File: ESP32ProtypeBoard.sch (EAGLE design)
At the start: 88 parts, among them IC2 SI4431BDY, J10 POWER_JACKPTH_LOCK, Q2 MMBT3904, Q3 MMBT3904, Q4 BSS138, U2 ESP-WROOM-32

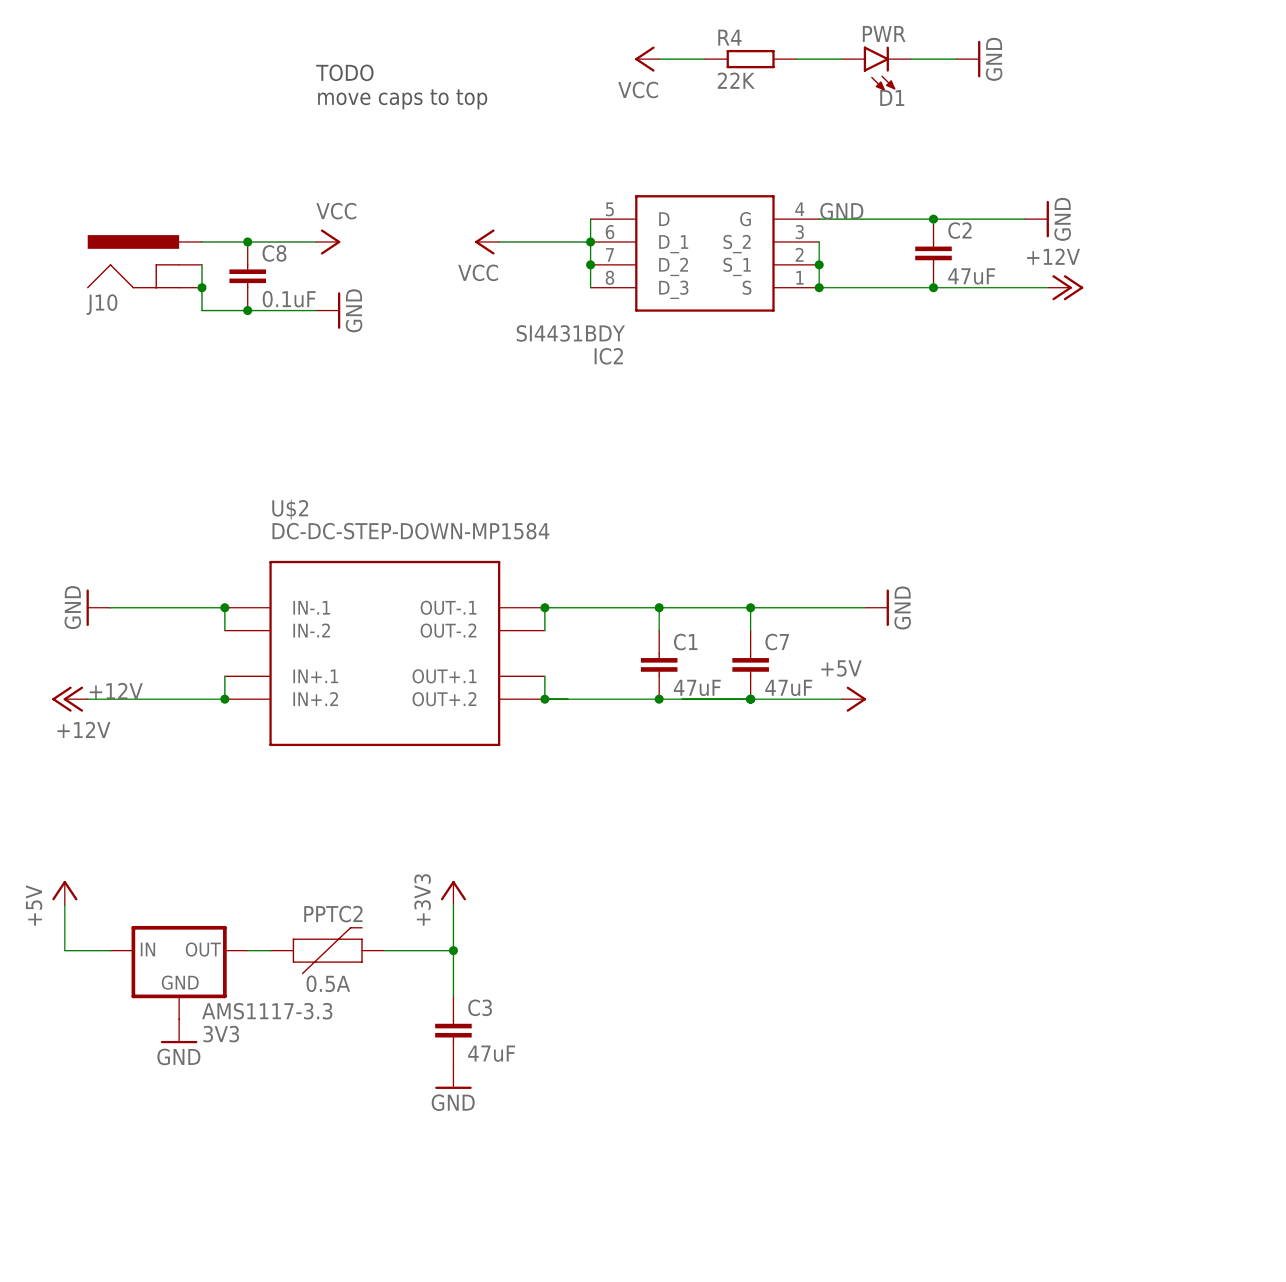
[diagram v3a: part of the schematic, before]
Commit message: Replaced buck converter module with custom curcuit
Using ACT4088US-T for 5V rail
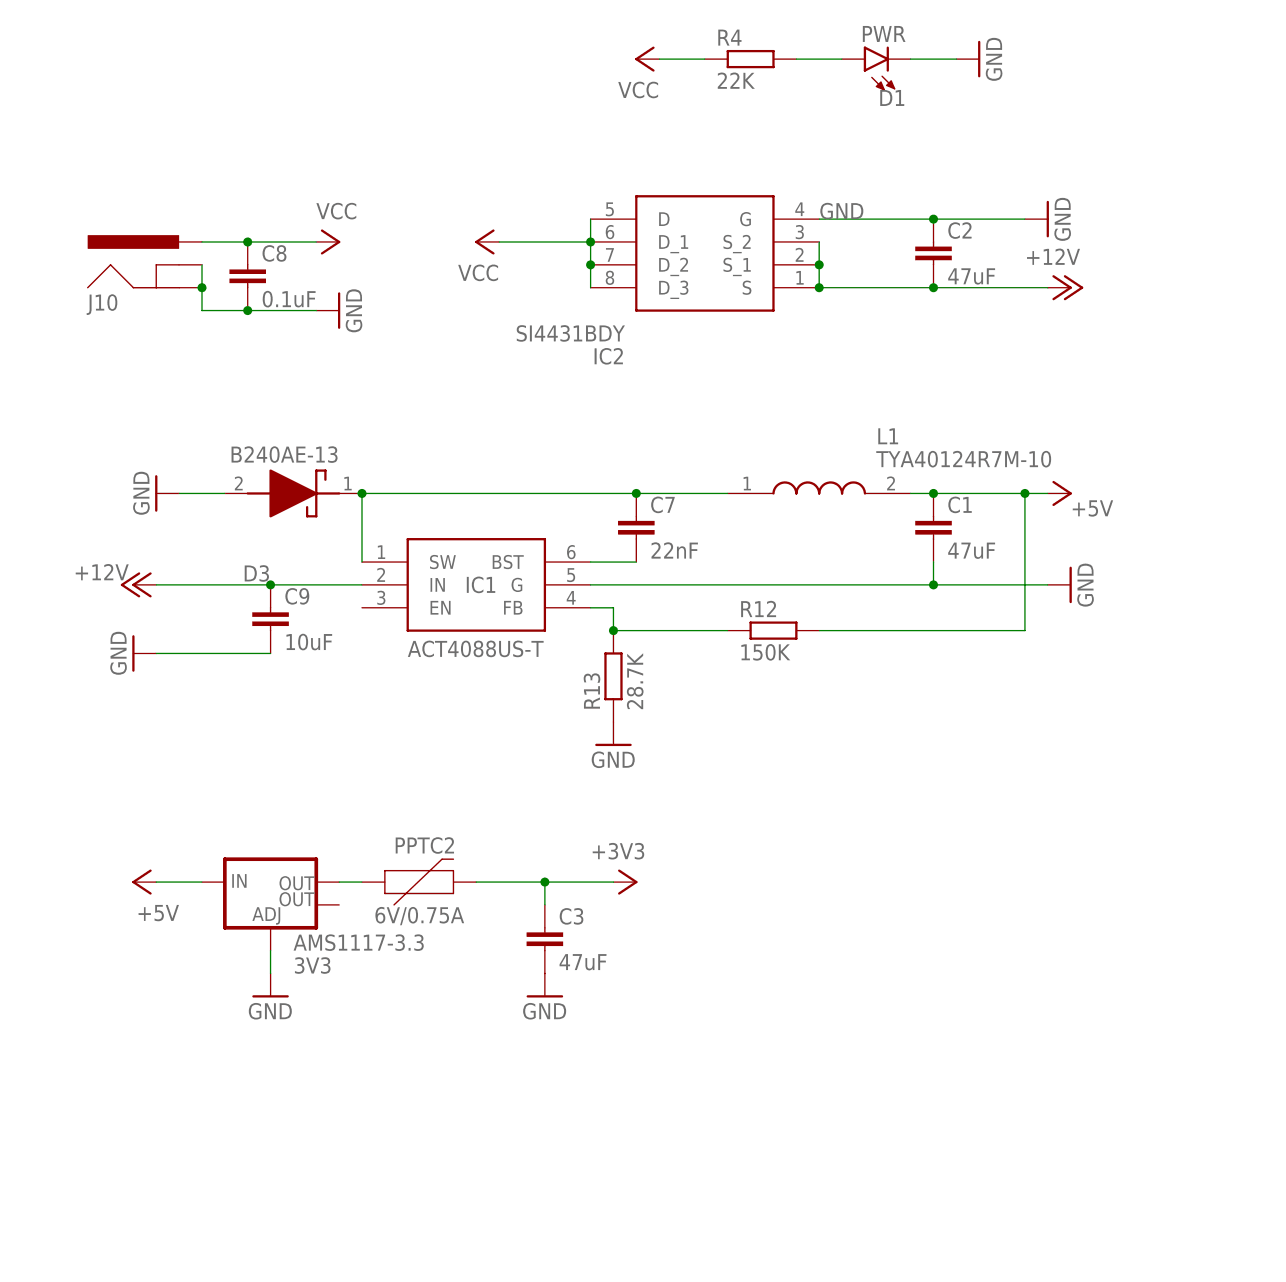
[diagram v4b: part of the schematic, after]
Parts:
- removed U$2: DC-DC-STEP-DOWN-MP1584, diy-modules-modified:DC-DC-STEP-DOWN-MP1584
- added C9: 10uF, rcl:C-EUC0805K
- added D3: B240AE-13, B240AE-13:B240AE-13
- added IC1: ACT4088US-T, ACT4088US-T:ACT4088US-T
- added L1: TYA40124R7M-10, TYA40124R7M-10:TYA40124R7M-10
- added R12: 150K, rcl:R-EU_R0805
- added R13: 28.7K, rcl:R-EU_R0805
- AMS1117-3.3: device SparkFun-IC-Power:V_REG_LD1117VXXLD1117-SMD -> SparkFun-IC-Power:V_REG_LM1117SOT223
- C7: value 47uF -> 22nF; device rcl:C-EUC1206K -> rcl:C-EUC0805K
- PPTC2: value 0.5A -> 6V/0.75A; device SparkFun-Fuses:PPTC_0.75A -> SparkFun-Fuses:PPTC_THREE-QUARTER-AMP
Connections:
- new net N$13: C7.1, D3.K, IC1.SW, L1.1
- new net N$14: C7.2, IC1.BST
- new net N$17: IC1.FB, R12.1, R13.2
- net +12V: now also C9.1, IC1.IN; no longer U$2.IN+.1, U$2.IN+.2
- net +5V: now also C1.1, L1.2, R12.2; no longer C1.2, C7.2, U$2.OUT+.1, U$2.OUT+.2
- net GND: now also AMS1117-3.3.ADJ, C1.2, C9.2, D3.A, IC1.G, R13.1; no longer AMS1117-3.3.GND, C1.1, C7.1, U$2.IN-.1, U$2.IN-.2, U$2.OUT-.1, U$2.OUT-.2
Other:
- note removed: "TODO move caps to top"
- moved on the sheet: C1, C3, C7

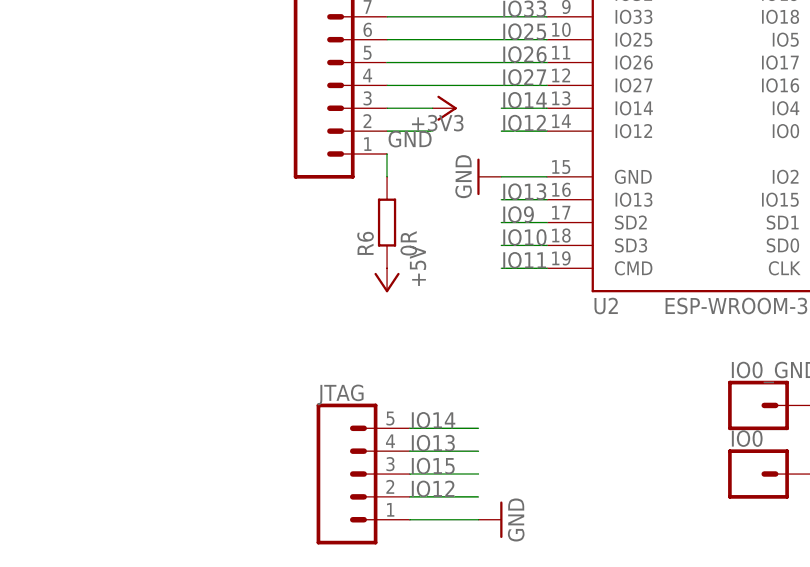
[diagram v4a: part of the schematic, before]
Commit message: Replaced all resistors with 0805 variants
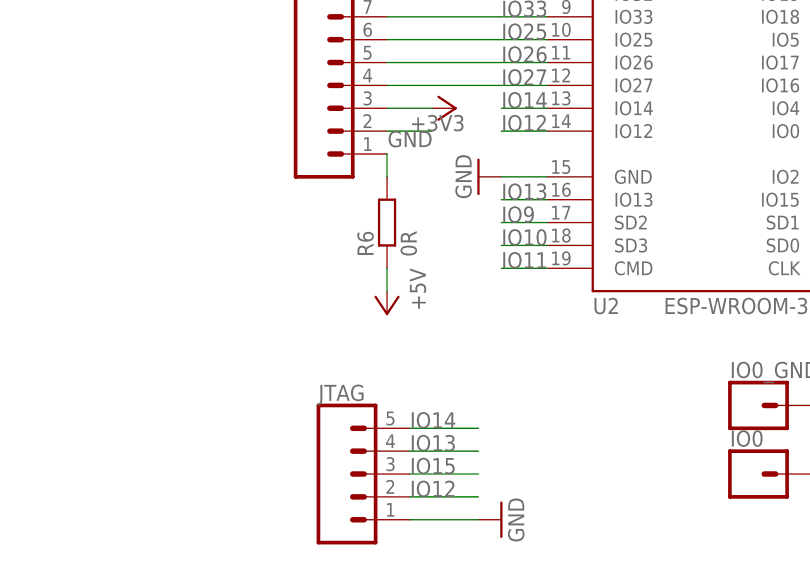
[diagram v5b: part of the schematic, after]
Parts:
- C4: device rcl:C-EUC1206 -> rcl:C-EUC0805K
- R1, R10, R11, R2, R3, R4, R5, R7, R8, R9: device eagle-ltspice:RR1206 -> rcl:R-EU_R0805
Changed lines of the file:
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@@
 <part name="GND2" library="supply1" library_urn="urn:adsk.eagle:library:371" deviceset="GND" device=""/>
 <part name="+3V1" library="supply1" library_urn="urn:adsk.eagle:library:371" deviceset="+3V3" device=""/>
-<part name="C4" library="rcl" library_urn="urn:adsk.eagle:library:334" deviceset="C-EU" device="C1206" package3d_urn="urn:adsk.eagle:package:23618/2" value="22uF"/>
+<part name="C4" library="rcl" library_urn="urn:adsk.eagle:library:334" deviceset="C-EU" device="C0805K" package3d_urn="urn:adsk.eagle:package:23681/2" value="22uF"/>
 <part name="C5" library="rcl" library_urn="urn:adsk.eagle:library:334" deviceset="C-EU" device="C0805K" package3d_urn="urn:adsk.eagle:package:23681/2" value="0.1uF"/>
-<part name="R5" library="eagle-ltspice" library_urn="urn:adsk.eagle:library:217" deviceset="R" device="R1206" package3d_urn="urn:adsk.eagle:package:13301/1" value="10K"/>
+<part name="R5" library="rcl" library_urn="urn:adsk.eagle:library:334" deviceset="R-EU_" device="R0805" package3d_urn="urn:adsk.eagle:package:23553/2" value="10K"/>
 <part name="C6" library="rcl" library_urn="urn:adsk.eagle:library:334" deviceset="C-EU" device="C0805K" package3d_urn="urn:adsk.eagle:package:23681/2" value="1nF"/>
 <part name="GND6" library="supply1" library_urn="urn:adsk.eagle:library:371" deviceset="GND" device=""/>
@@
 <part name="UART" library="SparkFun-Connectors" library_urn="urn:adsk.eagle:library:513" deviceset="CONN_06" device="LOCK" package3d_urn="urn:adsk.eagle:package:38002/1"/>
 <part name="GND20" library="supply1" library_urn="urn:adsk.eagle:library:371" deviceset="GND" device=""/>
-<part name="R7" library="eagle-ltspice" library_urn="urn:adsk.eagle:library:217" deviceset="R" device="R1206" package3d_urn="urn:adsk.eagle:package:13301/1" value="470R"/>
-<part name="R8" library="eagle-ltspice" library_urn="urn:adsk.eagle:library:217" deviceset="R" device="R1206" package3d_urn="urn:adsk.eagle:package:13301/1" value="470R"/>
+<part name="R7" library="rcl" library_urn="urn:adsk.eagle:library:334" deviceset="R-EU_" device="R0805" package3d_urn="urn:adsk.eagle:package:23553/2" value="470R"/>
+<part name="R8" library="rcl" library_urn="urn:adsk.eagle:library:334" deviceset="R-EU_" device="R0805" package3d_urn="urn:adsk.eagle:package:23553/2" value="470R"/>
 <part name="GND1" library="supply1" library_urn="urn:adsk.eagle:library:371" deviceset="GND" device=""/>
 <part name="AMS1117-3.3" library="SparkFun-IC-Power" library_urn="urn:adsk.eagle:library:526" deviceset="V_REG_LM1117" device="SOT223" package3d_urn="urn:adsk.eagle:package:39069/1" value="3V3"/>
@@
 <part name="P+8" library="supply1" library_urn="urn:adsk.eagle:library:371" deviceset="+12V" device=""/>
 <part name="D2" library="SparkFun-LED" deviceset="LED-GREEN" device="1206" value="GREEN"/>
-<part name="R1" library="eagle-ltspice" library_urn="urn:adsk.eagle:library:217" deviceset="R" device="R1206" package3d_urn="urn:adsk.eagle:package:13301/1" value="10K"/>
+<part name="R1" library="rcl" library_urn="urn:adsk.eagle:library:334" deviceset="R-EU_" device="R0805" package3d_urn="urn:adsk.eagle:package:23553/2" value="10K"/>
 <part name="J5" library="SparkFun-Connectors" library_urn="urn:adsk.eagle:library:513" deviceset="CONN_17" device="NOSILK" package3d_urn="urn:adsk.eagle:package:38192/1"/>
 <part name="J8" library="SparkFun-Connectors" library_urn="urn:adsk.eagle:library:513" deviceset="CONN_12" device="NO_SILK" package3d_urn="urn:adsk.eagle:package:38179/1"/>
-<part name="R2" library="eagle-ltspice" library_urn="urn:adsk.eagle:library:217" deviceset="R" device="R1206" package3d_urn="urn:adsk.eagle:package:13301/1" value="10K"/>
+<part name="R2" library="rcl" library_urn="urn:adsk.eagle:library:334" deviceset="R-EU_" device="R0805" package3d_urn="urn:adsk.eagle:package:23553/2" value="10K"/>
 <part name="+3V2" library="supply1" library_urn="urn:adsk.eagle:library:371" deviceset="+3V3" device=""/>
 <part name="P+11" library="supply1" library_urn="urn:adsk.eagle:library:371" deviceset="VCC" device=""/>
@@
 <part name="Q2" library="semicon-smd-ipc" library_urn="urn:adsk.eagle:library:353" deviceset="NPN-TRANSISTOR_" device="SOT23" package3d_urn="urn:adsk.eagle:package:28738/2" value="MMBT3904"/>
 <part name="Q3" library="semicon-smd-ipc" library_urn="urn:adsk.eagle:library:353" deviceset="NPN-TRANSISTOR_" device="SOT23" package3d_urn="urn:adsk.eagle:package:28738/2" value="MMBT3904"/>
-<part name="R3" library="eagle-ltspice" library_urn="urn:adsk.eagle:library:217" deviceset="R" device="R1206" package3d_urn="urn:adsk.eagle:package:13301/1" value="10K"/>
-<part name="R10" library="eagle-ltspice" library_urn="urn:adsk.eagle:library:217" deviceset="R" device="R1206" package3d_urn="urn:adsk.eagle:package:13301/1" value="10K"/>
+<part name="R3" library="rcl" library_urn="urn:adsk.eagle:library:334" deviceset="R-EU_" device="R0805" package3d_urn="urn:adsk.eagle:package:23553/2" value="10K"/>
+<part name="R10" library="rcl" library_urn="urn:adsk.eagle:library:334" deviceset="R-EU_" device="R0805" package3d_urn="urn:adsk.eagle:package:23553/2" value="10K"/>
 <part name="J56" library="SparkFun-Connectors" library_urn="urn:adsk.eagle:library:513" deviceset="CONN_11" device="1X11_NO_SILK" package3d_urn="urn:adsk.eagle:package:38260/1"/>
 <part name="J57" library="SparkFun-Connectors" library_urn="urn:adsk.eagle:library:513" deviceset="CONN_02" device="1X02_NO_SILK" package3d_urn="urn:adsk.eagle:package:38051/1"/>
 <part name="P+3" library="supply1" library_urn="urn:adsk.eagle:library:371" deviceset="VCC" device=""/>
-<part name="R4" library="eagle-ltspice" library_urn="urn:adsk.eagle:library:217" deviceset="R" device="R1206" package3d_urn="urn:adsk.eagle:package:13301/1" value="22K"/>
+<part name="R4" library="rcl" library_urn="urn:adsk.eagle:library:334" deviceset="R-EU_" device="R0805" package3d_urn="urn:adsk.eagle:package:23553/2" value="22K"/>
 <part name="D1" library="SparkFun-LED" deviceset="LED-GREEN" device="1206" value="PWR"/>
 <part name="GND5" library="supply1" library_urn="urn:adsk.eagle:library:371" deviceset="GND" device=""/>
@@
 <part name="SMD8" library="eagle-ltspice" library_urn="urn:adsk.eagle:library:217" deviceset="R" device="R1206" package3d_urn="urn:adsk.eagle:package:13301/1"/>
 <part name="Q1" library="semicon-smd-ipc" library_urn="urn:adsk.eagle:library:353" deviceset="NPN-TRANSISTOR_" device="SOT23" package3d_urn="urn:adsk.eagle:package:28738/2"/>
-<part name="R9" library="eagle-ltspice" library_urn="urn:adsk.eagle:library:217" deviceset="R" device="R1206" package3d_urn="urn:adsk.eagle:package:13301/1" value="100K"/>
+<part name="R9" library="rcl" library_urn="urn:adsk.eagle:library:334" deviceset="R-EU_" device="R0805" package3d_urn="urn:adsk.eagle:package:23553/2" value="100K"/>
 <part name="+3V6" library="supply1" library_urn="urn:adsk.eagle:library:371" deviceset="+3V3" device=""/>
 <part name="P+7" library="supply1" library_urn="urn:adsk.eagle:library:371" deviceset="+5V" device=""/>
@@
 <part name="GND14" library="supply1" library_urn="urn:adsk.eagle:library:371" deviceset="GND" device=""/>
 <part name="J2" library="SparkFun-Connectors" library_urn="urn:adsk.eagle:library:513" deviceset="CONN_03" device="LOCK_NO_SILK" package3d_urn="urn:adsk.eagle:package:38074/1"/>
-<part name="R11" library="eagle-ltspice" library_urn="urn:adsk.eagle:library:217" deviceset="R" device="R1206" package3d_urn="urn:adsk.eagle:package:13301/1" value="PULLUP21"/>
+<part name="R11" library="rcl" library_urn="urn:adsk.eagle:library:334" deviceset="R-EU_" device="R0805" package3d_urn="urn:adsk.eagle:package:23553/2" value="PULLUP21"/>
 <part name="J29" library="SparkFun-Connectors" deviceset="CONN_02" device="1X02_NO_SILK"/>
 <part name="J1" library="SparkFun-Connectors" library_urn="urn:adsk.eagle:library:513" deviceset="CONN_11" device="1X11_NO_SILK" package3d_urn="urn:adsk.eagle:package:38260/1"/>
@@
 <attribute name="VALUE" x="106.68" y="-35.56" size="1.778" layer="96"/>
 </instance>
-<instance part="P+9" gate="1" x="162.56" y="27.94" smashed="yes" rot="R180">
-<attribute name="VALUE" x="165.1" y="33.02" size="1.778" layer="96" rot="R270"/>
+<instance part="P+9" gate="1" x="162.56" y="25.4" smashed="yes" rot="R180">
+<attribute name="VALUE" x="165.1" y="30.48" size="1.778" layer="96" rot="R270"/>
 </instance>
 <instance part="+3V5" gate="G$1" x="231.14" y="50.8" smashed="yes" rot="R90">
@@
 <pinref part="P+9" gate="1" pin="+5V"/>
 <pinref part="R6" gate="G$1" pin="1"/>
-</segment>
-<segment>
+<wire x1="162.56" y1="27.94" x2="162.56" y2="30.48" width="0.1524" layer="91"/>
+</segment>
+<segment>

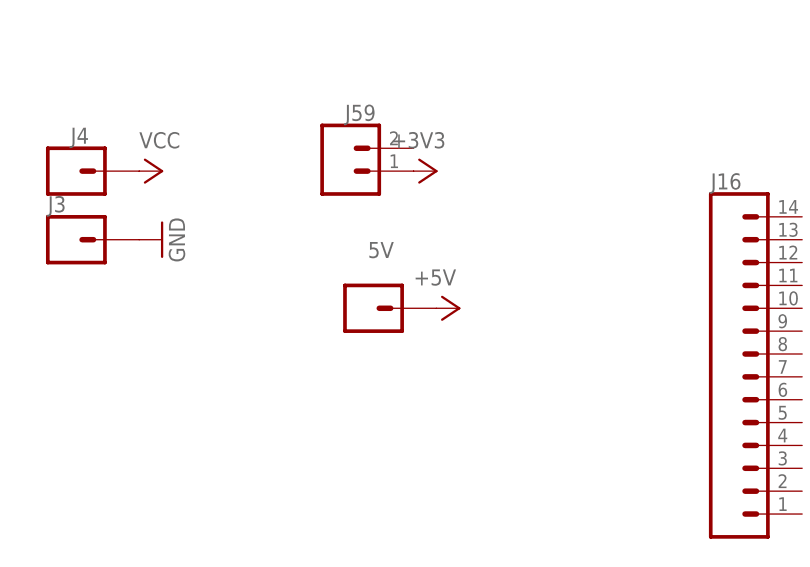
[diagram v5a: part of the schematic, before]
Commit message: Making layout smaller
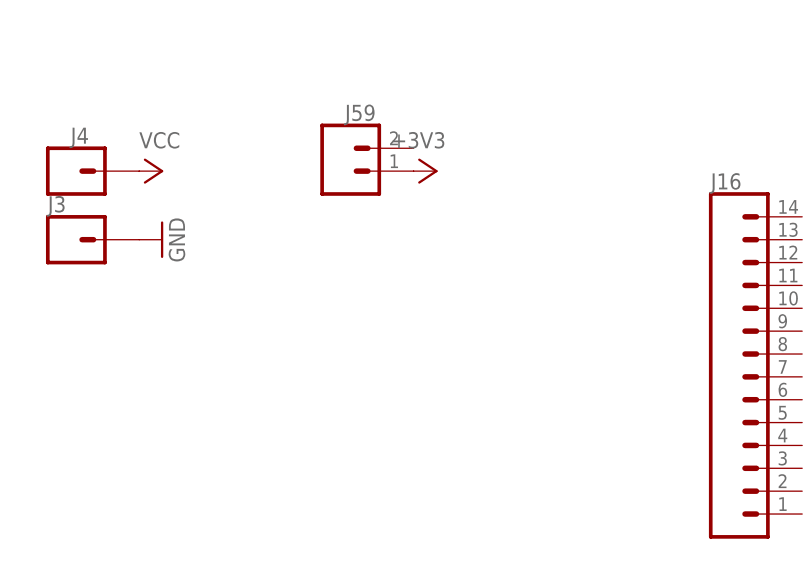
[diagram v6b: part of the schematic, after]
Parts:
- removed 5V: (no value), SparkFun-Connectors:CONN_01PTH_NO_SILK_KIT
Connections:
- net +5V: no longer 5V.1
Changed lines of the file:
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@@
 <part name="R9" library="rcl" library_urn="urn:adsk.eagle:library:334" deviceset="R-EU_" device="R0805" package3d_urn="urn:adsk.eagle:package:23553/2" value="100K"/>
 <part name="+3V6" library="supply1" library_urn="urn:adsk.eagle:library:371" deviceset="+3V3" device=""/>
-<part name="P+7" library="supply1" library_urn="urn:adsk.eagle:library:371" deviceset="+5V" device=""/>
-<part name="5V" library="SparkFun-Connectors" library_urn="urn:adsk.eagle:library:513" deviceset="CONN_01" device="PTH_NO_SILK_KIT" package3d_urn="urn:adsk.eagle:package:38038/1"/>
 <part name="+12V1" library="SparkFun-Connectors" deviceset="CONN_02" device="1X02_NO_SILK"/>
 <part name="GND10" library="supply1" library_urn="urn:adsk.eagle:library:371" deviceset="GND" device=""/>
@@
 <attribute name="VALUE" x="261.62" y="88.9" size="1.778" layer="96" rot="R270"/>
 </instance>
-<instance part="P+7" gate="1" x="114.3" y="-53.34" smashed="yes" rot="R270">
-<attribute name="VALUE" x="109.22" y="-50.8" size="1.778" layer="96"/>
-</instance>
-<instance part="5V" gate="G$1" x="104.14" y="-53.34" smashed="yes">
-<attribute name="VALUE" x="104.14" y="-53.086" size="1.778" layer="96" font="vector"/>
-<attribute name="NAME" x="104.14" y="-47.752" size="1.778" layer="95" font="vector"/>
-</instance>
 <instance part="+12V1" gate="G$1" x="17.78" y="-33.02" smashed="yes">
 <attribute name="VALUE" x="15.24" y="-37.846" size="1.778" layer="96" font="vector"/>
@@
 </segment>
 <segment>
-<pinref part="P+7" gate="1" pin="+5V"/>
-<pinref part="5V" gate="G$1" pin="1"/>
-</segment>
-<segment>

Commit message: TODO
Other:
- note added: "TODO prog interface TODO reset button replace TODO smaller diodes?"
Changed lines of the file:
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@@
 <sheet>
 <plain>
+<text x="-5.08" y="139.7" size="1.778" layer="91">TODO prog interface
+TODO reset button replace
+TODO smaller diodes?</text>
 </plain>
 <instances>
@@
 </drawing>
 <compatibility>
+<note version="6.3" minversion="6.2.2" severity="warning">
+Since Version 6.2.2 text objects can contain more than one line,
+which will not be processed correctly with this version.
+</note>
 <note version="8.2" severity="warning">
 Since Version 8.2, EAGLE supports online libraries. The ids
